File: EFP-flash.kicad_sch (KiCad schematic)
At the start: 23 parts, among them J101 USB_B_Micro, J102 USB_C_Receptacle_USB2.0, J103 Conn_01x06, Q101 MMDT3904, SW101 SW_SPDT, U101 ESD PROTECTION, U102 TLV75533PDBV, U103 CH340C

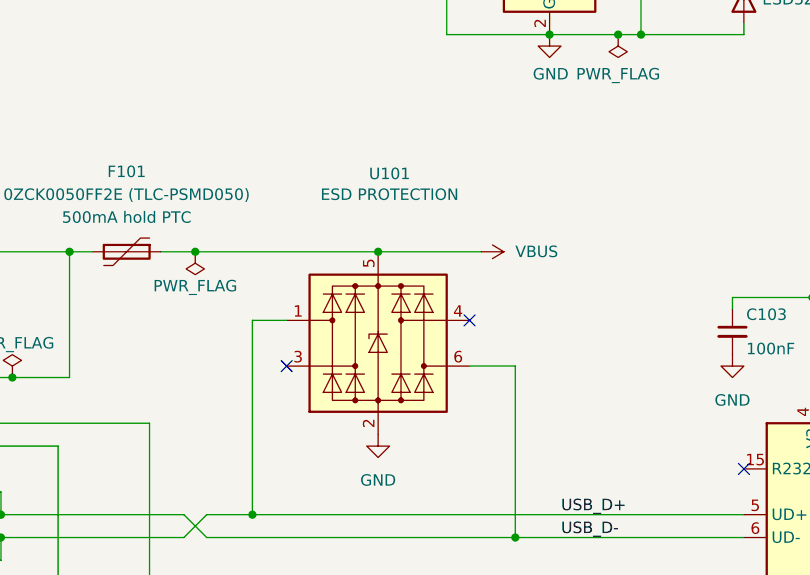
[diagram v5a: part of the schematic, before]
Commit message: squash! Sent to baord fab [1.1.0]
Made the ESD protection IC a library symbol.
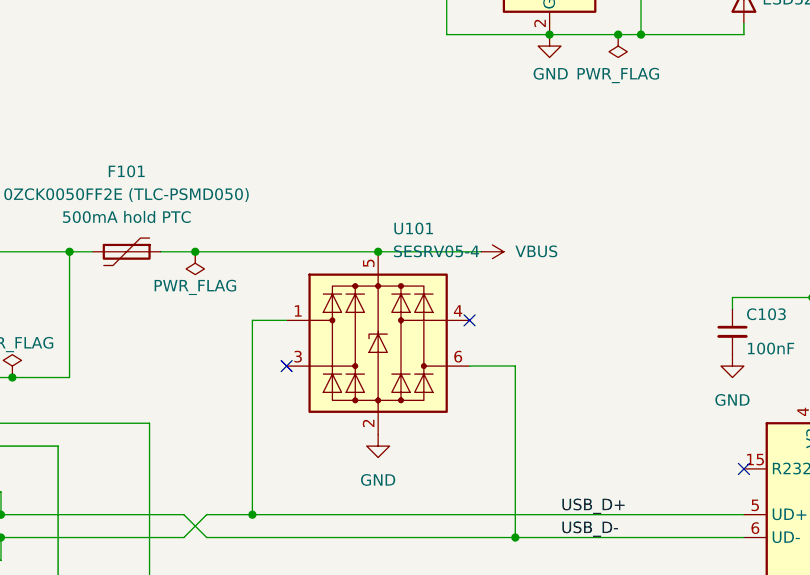
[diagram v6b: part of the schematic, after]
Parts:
- removed U101: ESD PROTECTION, Package_TO_SOT_SMD:SOT-23-6, symbol Power_Protection:USBLC6-4SC6
- added U101: SESRV05-4, Package_TO_SOT_SMD:SOT-23-6, symbol Power_Protection_custom:SESRV05-4
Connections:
- net GND: now also U101.2 (GND)
- net USB_D+: now also U101.1 (I/O1)
- net USB_D-: now also U101.6 (I/O4)
- net VBUS: now also U101.5 (VBUS)
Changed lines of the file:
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@@
   (junction (at 123.19 48.26) (diameter 0) (color 0 0 0 0)
   )
+  (junction (at 55.88 86.36) (diameter 0) (color 0 0 0 0)
+  )
+  (junction (at 62.23 72.39) (diameter 0) (color 0 0 0 0)
+  )
+  (junction (at 204.47 53.34) (diameter 0) (color 0 0 0 0)
+  )
+  (junction (at 125.73 48.26) (diameter 0) (color 0 0 0 0)
+  )
   (junction (at 96.52 72.39) (diameter 0) (color 0 0 0 0)
-  )
-  (junction (at 55.88 86.36) (diameter 0) (color 0 0 0 0)
-  )
-  (junction (at 62.23 72.39) (diameter 0) (color 0 0 0 0)
-  )
-  (junction (at 204.47 53.34) (diameter 0) (color 0 0 0 0)
-  )
-  (junction (at 125.73 48.26) (diameter 0) (color 0 0 0 0)
   )
   (junction (at 125.73 38.1) (diameter 0) (color 0 0 0 0)
@@
     (stroke (width 0) (type default))
   )
+  (wire (pts (xy 96.52 72.39) (xy 107.95 72.39))
+    (stroke (width 0) (type default))
+  )
   (wire (pts (xy 62.23 86.36) (xy 62.23 72.39))
     (stroke (width 0) (type default))
@@
   )
   (wire (pts (xy 204.47 125.73) (xy 204.47 128.27))
-    (stroke (width 0) (type default))
-  )
-  (wire (pts (xy 96.52 72.39) (xy 107.95 72.39))
     (stroke (width 0) (type default))
   )
@@
     )
   )
-  (symbol (lib_id "power:GND") (at 96.52 92.71 0) (unit 1)
-    (in_bom yes) (on_board yes) (dnp no) (fields_autoplaced)
-    (property "Reference" "#PWR0107" (at 96.52 99.06 0)
-      (effects (font (size 1.27 1.27)) hide)
-    )
-    (property "Value" "GND" (at 96.52 97.79 0)
-      (effects (font (size 1.27 1.27)))
-    )
-    (property "Footprint" "" (at 96.52 92.71 0)
-      (effects (font (size 1.27 1.27)) hide)
-    )
-    (property "Datasheet" "" (at 96.52 92.71 0)
-      (effects (font (size 1.27 1.27)) hide)
-    )
-    (pin "1")
-    (instances
-      (project "EFP-flash"
-        (path "/a623f881-bf21-4f21-bf99-f5c7db3a5968"
-          (reference "#PWR0107") (unit 1)
-        )
-      )
-    )
-  )
-  (symbol (lib_id "power:GND") (at 152.4 83.82 0) (unit 1)
-    (in_bom yes) (on_board yes) (dnp no) (fields_autoplaced)
-    (property "Reference" "#PWR0115" (at 152.4 90.17 0)
-      (effects (font (size 1.27 1.27)) hide)
-    )
-    (property "Value" "GND" (at 152.4 88.9 0)
-      (effects (font (size 1.27 1.27)))
-    )
-    (property "Footprint" "" (at 152.4 83.82 0)
-      (effects (font (size 1.27 1.27)) hide)
-    )
-    (property "Datasheet" "" (at 152.4 83.82 0)
-      (effects (font (size 1.27 1.27)) hide)
-    )
-    (pin "1")
-    (instances
-      (project "EFP-flash"
-        (path "/a623f881-bf21-4f21-bf99-f5c7db3a5968"
-          (reference "#PWR0115") (unit 1)
-        )
-      )
-    )
-  )
-  (symbol (lib_id "Power_Protection:USBLC6-4SC6") (at 96.52 82.55 0) (unit 1)
-    (in_bom yes) (on_board yes) (dnp no)
-    (property "Reference" "U101" (at 97.79 63.7286 0)
-      (effects (font (size 1.27 1.27)))
-    )
-    (property "Value" "ESD PROTECTION" (at 97.79 66.04 0)
-      (effects (font (size 1.27 1.27)))
+  (symbol (lib_id "Power_Protection_custom:SESRV05-4") (at 96.52 82.55 0) (unit 1)
+    (in_bom yes) (on_board yes) (dnp no) (fields_autoplaced)
+    (property "Reference" "U101" (at 98.1711 69.85 0)
+      (effects (font (size 1.27 1.27)) (justify left))
+    )
+    (property "Value" "SESRV05-4" (at 98.1711 72.39 0)
+      (effects (font (size 1.27 1.27)) (justify left))
     )
     (property "Footprint" "Package_TO_SOT_SMD:SOT-23-6" (at 96.52 95.25 0)
       (effects (font (size 1.27 1.27)) hide)
     )
-    (property "Datasheet" "https://www.st.com/resource/en/datasheet/usblc6-4.pdf" (at 101.6 73.66 0)
+    (property "Datasheet" "https://datasheet.lcsc.com/lcsc/1912111437_SEMIWARE-SESRV05-4_C294963.pdf" (at 101.6 73.66 0)
       (effects (font (size 1.27 1.27)) hide)
     )
@@
         )
       )
+    )
+  )
+  (symbol (lib_id "power:GND") (at 96.52 92.71 0) (unit 1)
+    (in_bom yes) (on_board yes) (dnp no) (fields_autoplaced)
+    (property "Reference" "#PWR0107" (at 96.52 99.06 0)
+      (effects (font (size 1.27 1.27)) hide)
+    )
+    (property "Value" "GND" (at 96.52 97.79 0)
+      (effects (font (size 1.27 1.27)))
+    )
+    (property "Footprint" "" (at 96.52 92.71 0)
+      (effects (font (size 1.27 1.27)) hide)
+    )
+    (property "Datasheet" "" (at 96.52 92.71 0)
+      (effects (font (size 1.27 1.27)) hide)
+    )
+    (pin "1")
+    (instances
+      (project "EFP-flash"
+        (path "/a623f881-bf21-4f21-bf99-f5c7db3a5968"
+          (reference "#PWR0107") (unit 1)
+        )
+      )
+    )
+  )
+  (symbol (lib_id "power:GND") (at 152.4 83.82 0) (unit 1)
+    (in_bom yes) (on_board yes) (dnp no) (fields_autoplaced)
+    (property "Reference" "#PWR0115" (at 152.4 90.17 0)
+      (effects (font (size 1.27 1.27)) hide)
+    )
+    (property "Value" "GND" (at 152.4 88.9 0)
+      (effects (font (size 1.27 1.27)))
+    )
+    (property "Footprint" "" (at 152.4 83.82 0)
+      (effects (font (size 1.27 1.27)) hide)
+    )
+    (property "Datasheet" "" (at 152.4 83.82 0)
+      (effects (font (size 1.27 1.27)) hide)
+    )
+    (pin "1")
+    (instances
+      (project "EFP-flash"
+        (path "/a623f881-bf21-4f21-bf99-f5c7db3a5968"
+          (reference "#PWR0115") (unit 1)
+        )
+      )
